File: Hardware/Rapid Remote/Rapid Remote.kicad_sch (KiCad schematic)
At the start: 42 parts, among them J1 Conn_01x02_Socket, U1 MIC5504-3.3YM5, U2 ESP32-C3-MINI-1-N4, U3 WS4518D, U4 XB6096I2SV

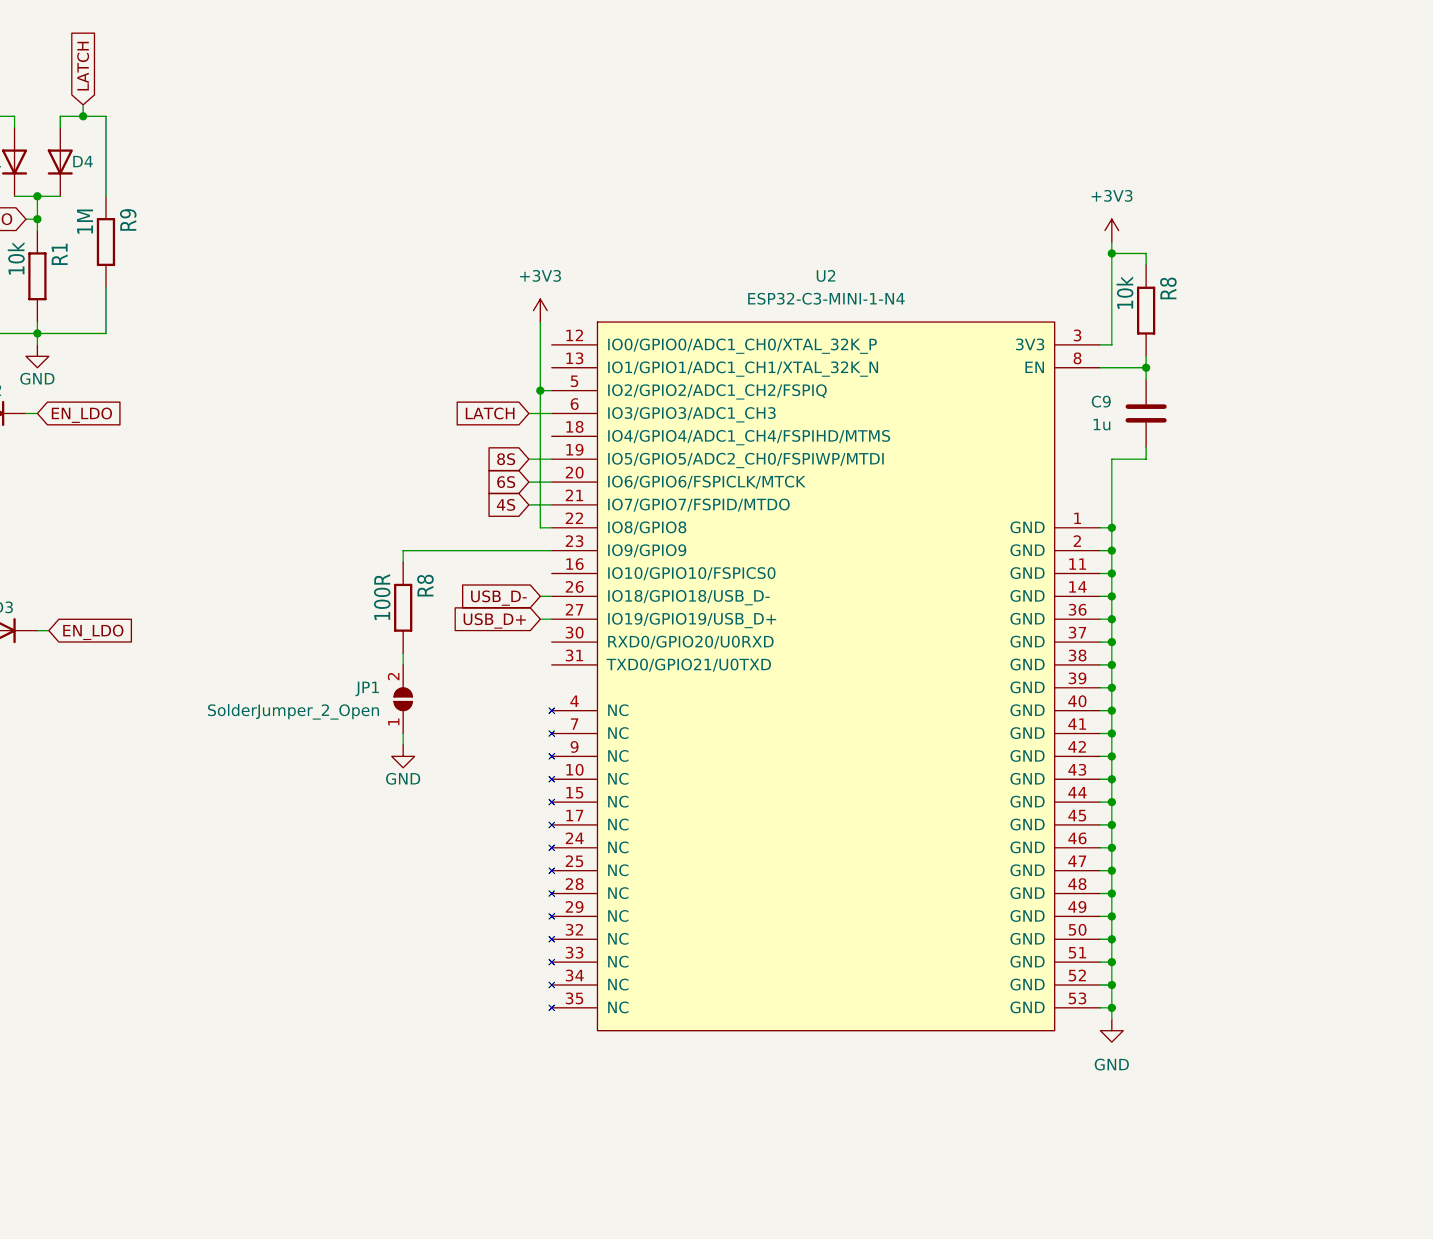
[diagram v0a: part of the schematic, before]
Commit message: added boot and reset buttons
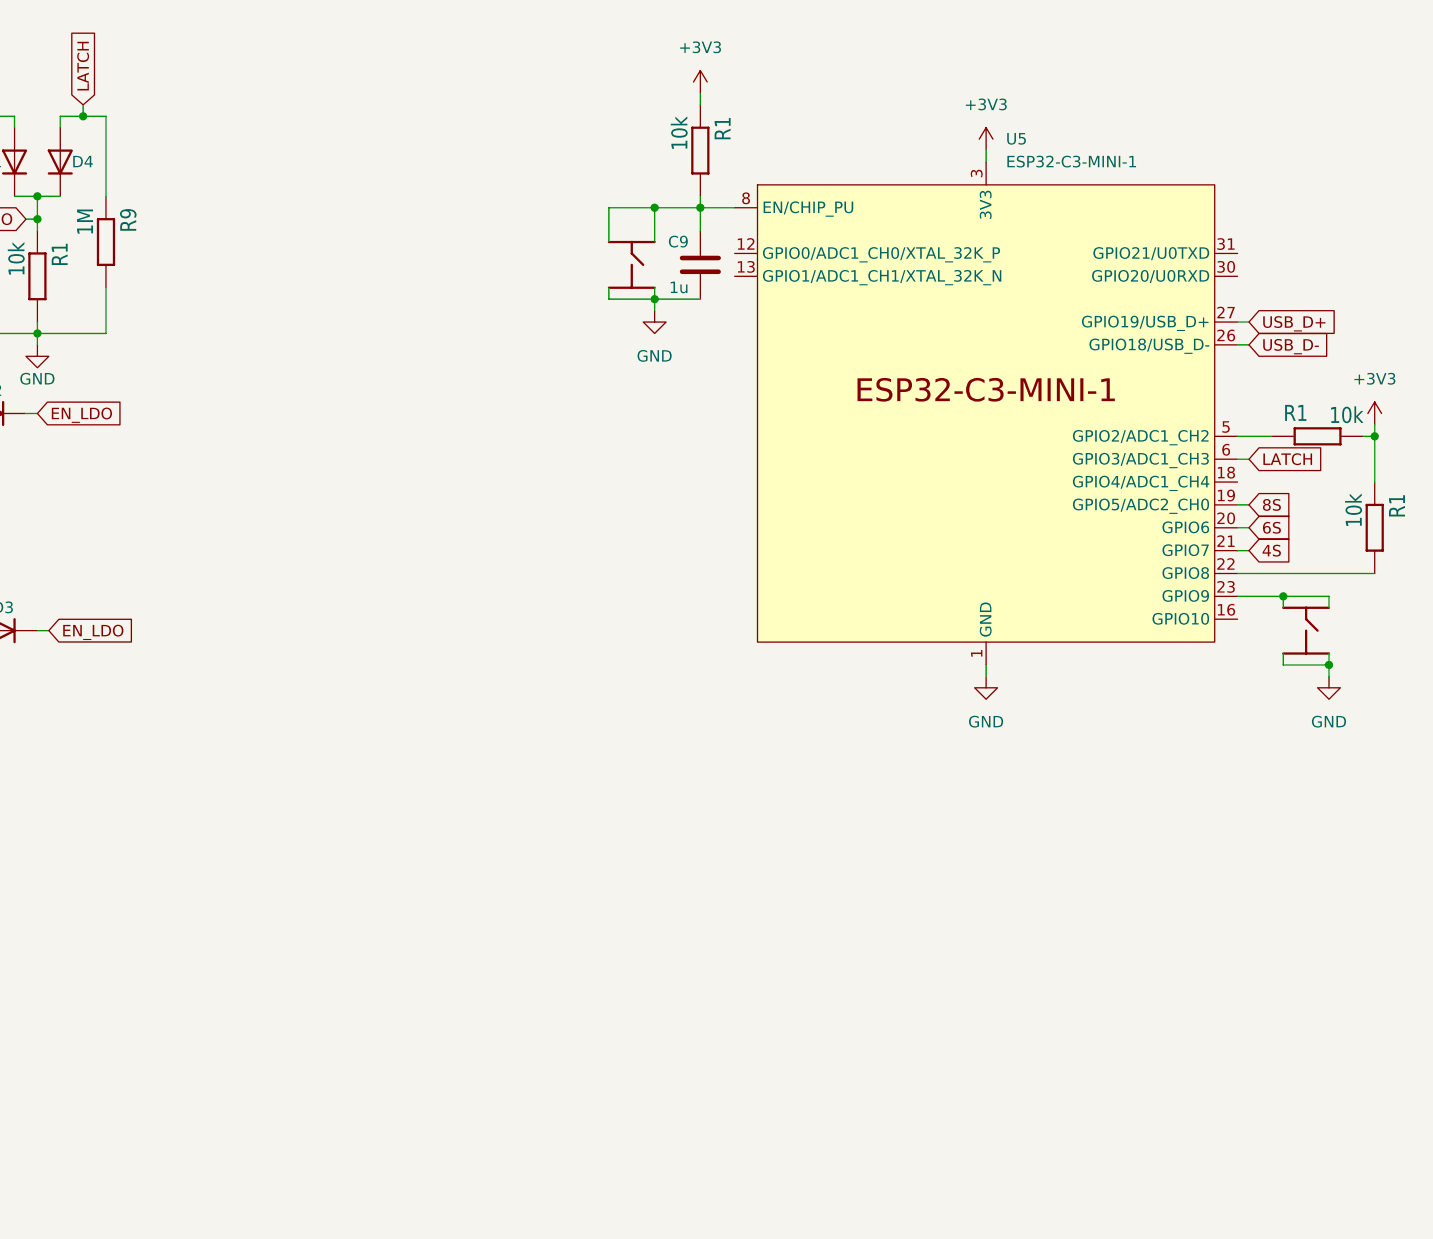
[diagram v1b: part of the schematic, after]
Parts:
- removed JP1: SolderJumper_2_Open, Jumper:SolderJumper-2_P1.3mm_Open_RoundedPad1.0x1.5mm, symbol Jumper:SolderJumper_2_Open
- removed R8: 10k, Resistor_SMD:R_0603_1608Metric, symbol picoclick_c3_v1.1-eagle-import:moekoe_rcl_R0402
- removed R8: 100R, Resistor_SMD:R_0603_1608Metric, symbol picoclick_c3_v1.1-eagle-import:moekoe_rcl_R0402
- removed U2: ESP32-C3-MINI-1-N4, Personal:ESP32-­C3-­MINI­-1, symbol personal2:ESP32-­C3-­MINI­-1
- added R1 (x3): 10k, Resistor_SMD:R_0603_1608Metric, symbol picoclick_c3_v1.1-eagle-import:moekoe_rcl_R0402
- added U5: ESP32-C3-MINI-1, PCM_Espressif:ESP32-C3-MINI-1, symbol PCM_Espressif:ESP32-C3-MINI-1
- added s1, s2: BUTTON_4PIN_TS_1177, rapidtraining:TS-1177-C-B-B, symbol personal2:BUTTON_4PIN_TS_1177
- s4, s6, s8: footprint Personal:TS-1177-C-B-B -> rapidtraining:TS-1177-C-B-B
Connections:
- net +3V3: now also R1.1, R1.1, R1.2, U5.3 (3V3)
- net 4S: now also U5.21 (GPIO7)
- net 6S: now also U5.20 (GPIO6)
- net 8S: now also U5.19 (GPIO5/ADC2_CH0)
- net GND: now also U5.1 (GND), U5.11 (GND), U5.14 (GND), U5.2 (GND), U5.36 (GND), U5.37 (GND), U5.38 (GND), U5.39 (GND), U5.40 (GND), U5.41 (GND), U5.42 (GND), U5.43 (GND), U5.44 (GND), U5.45 (GND), U5.46 (GND), U5.47 (GND), U5.48 (GND), U5.49 (GND), U5.50 (GND), U5.51 (GND), U5.52 (GND), U5.53 (GND), s1.P3 (3), s1.P4 (4), s2.P3 (3), s2.P4 (4)
- net LATCH: now also U5.6 (GPIO3/ADC1_CH3)
- net USB_D+: now also U5.27 (GPIO19/USB_D+)
- net USB_D-: now also U5.26 (GPIO18/USB_D-)
- net at C9.1: now also R1.2, U5.8 (EN/CHIP_PU), s1.P1 (1), s1.P2 (2)
- new net: U5.23 (GPIO9), s2.P1 (1), s2.P2 (2)
- new net: R1.2, U5.22 (GPIO8)
- new net: R1.1, U5.5 (GPIO2/ADC1_CH2)
